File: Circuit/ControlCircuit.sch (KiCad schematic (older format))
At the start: 3 parts

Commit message: Schematics and PCB work
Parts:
- added C101: 4uF, Capacitors_SMD:C_0805, symbol CP1
- added C102: 32pF, Capacitors_SMD:C_0805, symbol C
- added C103: CP1, symbol CP1
- added D101: D_Schottky, symbol D_Schottky
- added L101: 260mH, symbol L
- added R101: 18kR, Resistors_SMD:R_0805, symbol R
- added R102: 11kR, Resistors_SMD:R_0805, symbol R
- added R103: 1.5R, Resistors_SMD:R_0805, symbol R
- added VR101: MC34063A, symbol MC34063A
- IC101: renamed from IC?; footprint DIL28 -> Housings_DIP:DIP-28_W7.62mm
- LCD101: renamed from LCD?; footprint (none) -> Pin_Headers:Pin_Header_Straight_2x20_Pitch2.54mm
- R104: renamed from R?; footprint (none) -> Resistors_SMD:R_0805
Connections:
- net GNDREF is gone; now on net GND: LCD101.1 (LEDK), LCD101.10 (DB15), LCD101.11 (DB14), LCD101.12 (DB13), LCD101.13 (DB12), LCD101.14 (DB11), LCD101.15 (DB10), LCD101.16 (DB9), LCD101.17 (DB8), LCD101.18 (DB7), LCD101.19 (DB6), LCD101.20 (DB5), LCD101.21 (DB4), LCD101.22 (DB3), LCD101.23 (DB2), LCD101.24 (DB1), LCD101.25 (DB0), LCD101.26 (GND), LCD101.8 (DB17), LCD101.9 (DB16)
- net +3V3: now also LCD101.39 (3.3V), LCD101.4 (IM3), LCD101.5 (IM2), LCD101.6 (IM1), C101.1, D101.1 (K), L101.1, VR101.2 (Switch_Emitter)
- net CS: now also LCD101.32 (CS)
- net MISO: now also LCD101.27 (SDO)
- net MOSI: now also LCD101.28 (SDI)
- net SCK: now also LCD101.31 (RS)
- net WR: now also LCD101.30 (WR)
- net GND: now reaches LCD101.29 (RD)
- net GND: now also LCD101.3 (IM0), LCD101.33 (TE), LCD101.34 (GND), LCD101.40 (GND), C101.2, C102.1, C103.2, D101.2 (A), R102.1, VR101.4 (Grid)
- net X+: now reaches LCD101.35 (X+)
- net Y+: now reaches LCD101.36 (Y+)
- net X-: now reaches LCD101.37 (X-)
- net Y-: now reaches LCD101.38 (Y-)
- net RST: now reaches LCD101.7 (RST)
- new net: R103.2, VR101.1 (Switch_Collector), VR101.7 (Ipk_Sense), VR101.8 (Driver_Collector)
- new net: C102.2, VR101.3 (Timing_Capacitor)
- new net: R101.1, R102.2, VR101.5 (Comp_Inv_Input)
- new net: L101.2, R101.2
- new net +24V: R103.1, VR101.6 (Vcc)
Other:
- note added: "LCD + Touch screen"
- note added: "Relay Inputs, contains \nglobal labels Input1..6"
- note added: "Relay Outputs, contains \nglobal labels Output1..6"
- note added: "Voltage regulation and power supply"
- moved on the sheet: IC101, LCD101, R104

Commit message: Continued PCB work, placement started. Report and presentation also started
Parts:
- C103: value CP1 -> 100uF; footprint (none) -> Capacitors_SMD:C_0805
- D101: footprint (none) -> Diodes_SMD:D_0805
- L101: footprint (none) -> Inductors:Inductor_1212
- VR101: footprint (none) -> Housings_DIP:DIP-8_W7.62mm
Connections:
- net +24V: now also C103.1
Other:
- moved on the sheet: C103
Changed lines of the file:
@@
 EESchema Schematic File Version 2
+LIBS:ControlCircuit-rescue
 LIBS:power
 LIBS:device
@@
 F 0 "VR101" H 9100 4750 60  0000 C CNN
 F 1 "MC34063A" H 9100 4150 60  0000 C CNN
-F 2 "" H 8200 4600 60  0001 C CNN
+F 2 "Housings_DIP:DIP-8_W7.62mm" H 8200 4600 60  0001 C CNN
 F 3 "" H 8200 4600 60  0001 C CNN
 	1    9100 4450
@@
 F 0 "L101" V 8500 5100 50  0000 C CNN
 F 1 "260mH" V 8625 5100 50  0000 C CNN
-F 2 "" H 8550 5100 50  0001 C CNN
+F 2 "Inductors:Inductor_1212" H 8550 5100 50  0001 C CNN
 F 3 "" H 8550 5100 50  0000 C CNN
 	1    8550 5100
@@
 L CP1 C103
 U 1 1 58ADC4C2
-P 10300 4650
-F 0 "C103" H 10325 4750 50  0000 L CNN
-F 1 "CP1" H 10325 4550 50  0000 L CNN
-F 2 "" H 10300 4650 50  0001 C CNN
-F 3 "" H 10300 4650 50  0000 C CNN
-	1    10300 4650
+P 10300 4750
+F 0 "C103" H 10325 4850 50  0000 L CNN
+F 1 "100uF" H 10325 4650 50  0000 L CNN
+F 2 "Capacitors_SMD:C_0805" H 10300 4750 50  0001 C CNN
+F 3 "" H 10300 4750 50  0000 C CNN
+	1    10300 4750
 	1    0    0    -1
 $EndComp
@@
 F 0 "D101" H 7400 4500 50  0000 C CNN
 F 1 "D_Schottky" H 7400 4300 50  0000 C CNN
-F 2 "" H 7400 4400 50  0001 C CNN
+F 2 "Diodes_SMD:D_0805" H 7400 4400 50  0001 C CNN
 F 3 "" H 7400 4400 50  0000 C CNN
 	1    7400 4400
@@
 L GND #PWR012
 U 1 1 58ADCA05
-P 10300 4800
-F 0 "#PWR012" H 10300 4550 50  0001 C CNN
-F 1 "GND" H 10300 4650 50  0000 C CNN
-F 2 "" H 10300 4800 50  0000 C CNN
-F 3 "" H 10300 4800 50  0000 C CNN
-	1    10300 4800
+P 10300 5000
+F 0 "#PWR012" H 10300 4750 50  0001 C CNN
+F 1 "GND" H 10300 4850 50  0000 C CNN
+F 2 "" H 10300 5000 50  0000 C CNN
+F 3 "" H 10300 5000 50  0000 C CNN
+	1    10300 5000
 	1    0    0    -1
 $EndComp
@@
 Wire Notes Line
 	3650 650  2450 650
+Wire Wire Line
+	10300 4600 10300 4500
+Connection ~ 10300 4500
+Wire Wire Line
+	10300 4900 10300 5000
 $EndSCHEMATC

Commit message: Continued PCB work, additional footprints added
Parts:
- removed IC101: ATMEGA328-P, Housings_DIP:DIP-28_W7.62mm, symbol ATMEGA328-P
- removed LCD101: tft-proto-mi0283qt-9a, Pin_Headers:Pin_Header_Straight_2x20_Pitch2.54mm, symbol tft-proto-mi0283qt-9a
- removed R104: 100R, Resistors_SMD:R_0805, symbol R
- D101: footprint Diodes_SMD:D_0805 -> Diodes_SMD:D_MiniMELF_Standard
- L101: footprint Inductors:Inductor_1212 -> Inductors:Inductor_Wurth_HCI-7050
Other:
- note removed: "LCD + Touch screen"
- note removed: "Relay Inputs, contains \nglobal labels Input1..6"
- note removed: "Relay Outputs, contains \nglobal labels Output1..6"

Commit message: Additional PCB work
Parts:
- added P101, P102, P103, P104: CONN_01X08, Connectors_Terminal_Blocks:TerminalBlock_Pheonix_MKDS1.5-8pol, symbol CONN_01X08
- added P105: CONN_01X02, Connectors_Terminal_Blocks:TerminalBlock_Pheonix_MKDS1.5-2pol, symbol CONN_01X02
- VR101: footprint Housings_DIP:DIP-8_W7.62mm -> Housings_SOIC:SOIC-8_3.9x4.9mm_Pitch1.27mm
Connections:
- net labels added: OR6s1, OR6s2, OR7c, OR7s2, OR8c, OR8s2
- wire segments 28 -> 127

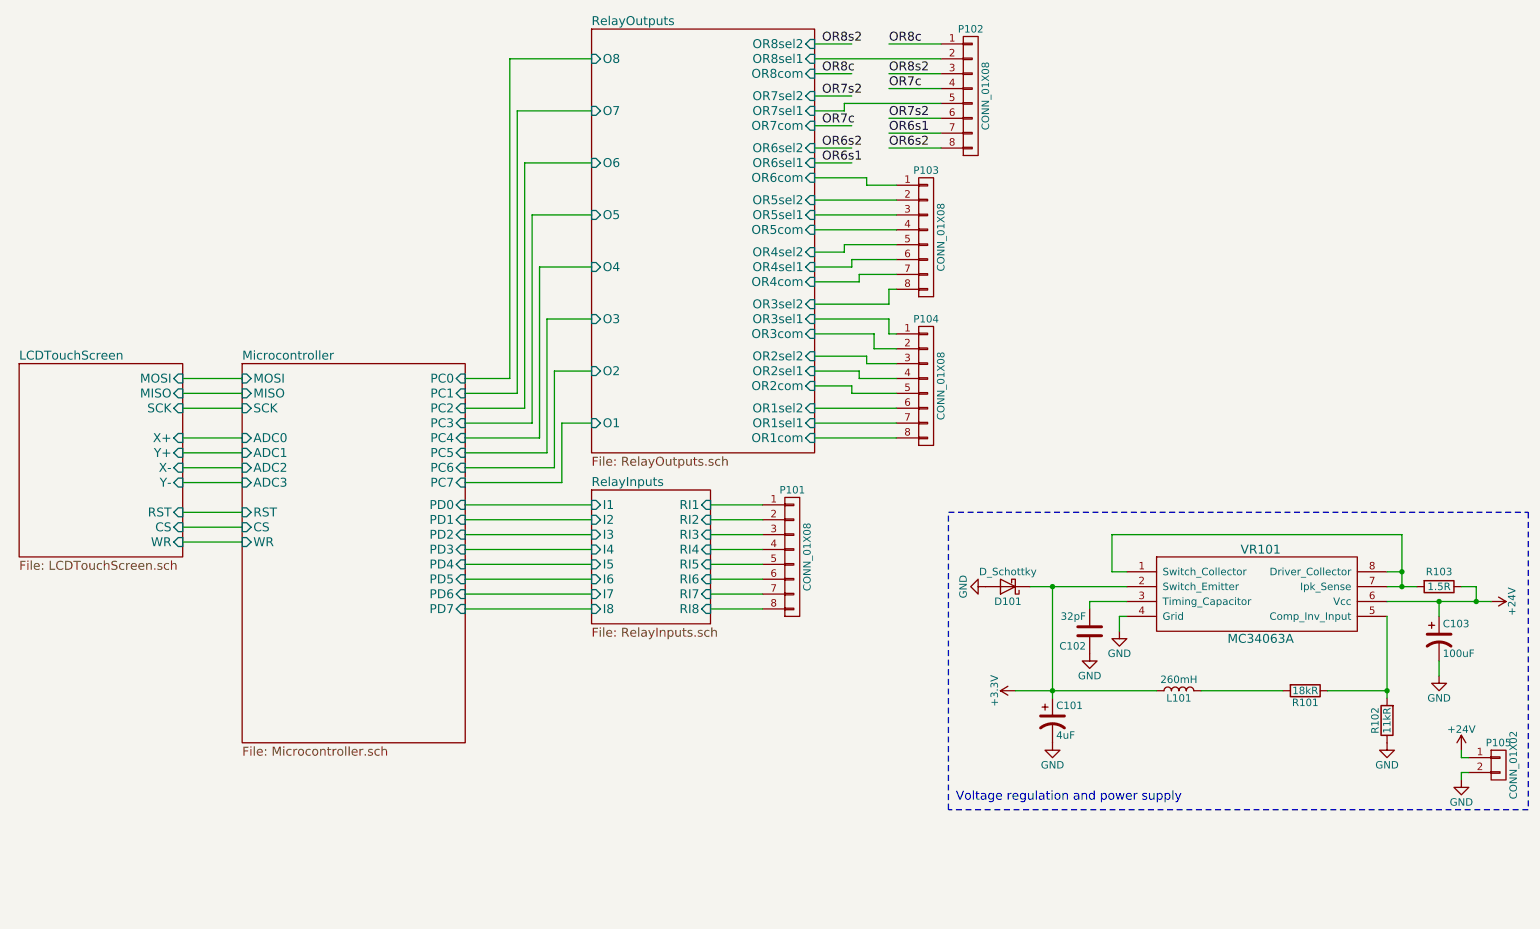
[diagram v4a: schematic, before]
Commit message: Routed PCB and made backup. Footprint for Optocouplers
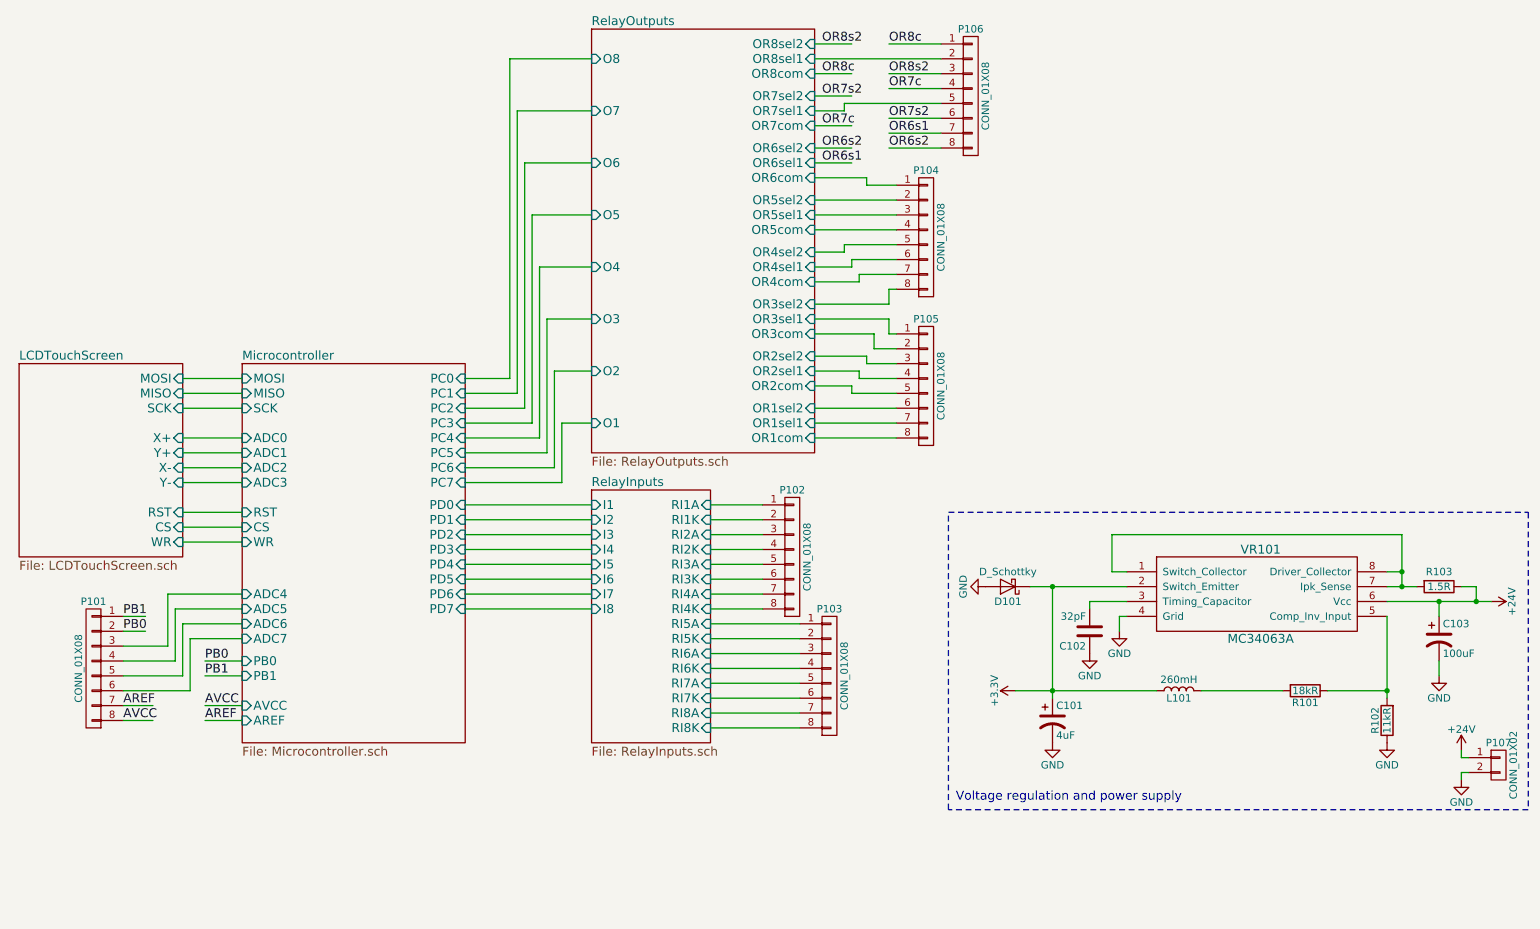
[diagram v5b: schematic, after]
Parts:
- added P101, P103: CONN_01X08, Connectors_Terminal_Blocks:TerminalBlock_Pheonix_MKDS1.5-8pol, symbol CONN_01X08
- renumbered P101 to P102, P103 to P104, P104 to P105, P102 to P106, P105 to P107
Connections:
- net labels added: AREF, AVCC, PB0, PB1
- wire segments 127 -> 155

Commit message: PCB. Pours mostly complete. Almost done?
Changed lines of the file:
@@
 F 3 "" H 10700 5600 50  0000 C CNN
 	1    10700 5600
-	1    0    0    -1
+	1    0    0    1
 $EndComp
 $Comp

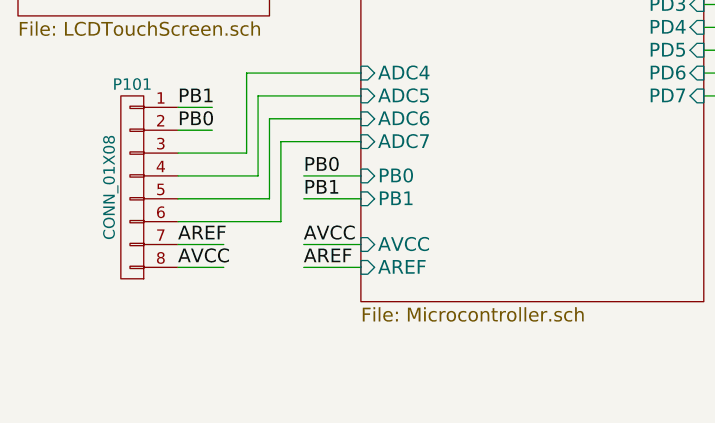
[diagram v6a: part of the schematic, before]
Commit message: Cleaned up silkscreen. Everything connected.
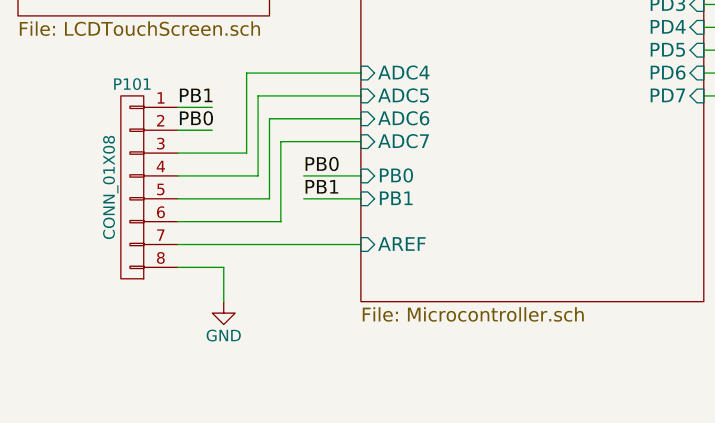
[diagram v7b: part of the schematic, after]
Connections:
- net labels removed: AREF, AVCC
- wire segments 155 -> 154
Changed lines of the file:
@@
 F32 "PB0" I L 2250 4900 60
 F33 "PB1" I L 2250 5000 60
-F34 "AVCC" I L 2250 5200 60
-F35 "AREF" I L 2250 5300 60
+F34 "AREF" I L 2250 5200 60
 $EndSheet
 $Comp
@@
 	1750 4800 1450 4800
 Wire Wire Line
-	1450 5200 1650 5200
+	1450 5200 2250 5200
 Wire Wire Line
 	1450 5300 1650 5300
 Wire Wire Line
-	2250 5200 2000 5200
-Wire Wire Line
-	2250 5300 2000 5300
-Text Label 2000 5200 0    60   ~ 0
-AVCC
-Text Label 2000 5300 0    60   ~ 0
-AREF
-Text Label 1450 5200 0    60   ~ 0
-AREF
-Text Label 1450 5300 0    60   ~ 0
-AVCC
+	1650 5300 1650 5450
+$Comp
+L GND #PWR?
+U 1 1 58B98A53
+P 1650 5450
+F 0 "#PWR?" H 1650 5200 50  0001 C CNN
+F 1 "GND" H 1650 5300 50  0000 C CNN
+F 2 "" H 1650 5450 50  0000 C CNN
+F 3 "" H 1650 5450 50  0000 C CNN
+	1    1650 5450
+	1    0    0    -1
+$EndComp
 $EndSCHEMATC

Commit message: PCB Revision 1
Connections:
- net labels added: PB3, PB4
- net labels removed: PB0, PB1
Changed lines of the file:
@@
 F30 "ADC6" I L 2250 4650 60
 F31 "ADC7" I L 2250 4750 60
-F32 "PB0" I L 2250 4900 60
-F33 "PB1" I L 2250 5000 60
-F34 "AREF" I L 2250 5200 60
+F32 "AREF" I L 2250 5200 60
+F33 "PB3" I L 2250 4900 60
+F34 "PB4" I L 2250 5000 60
 $EndSheet
 $Comp
@@
 Wire Wire Line
 	1450 4600 1600 4600
+Text Label 1450 4600 0    60   ~ 0
+PB4
 Text Label 1450 4700 0    60   ~ 0
-PB0
-Text Label 1450 4600 0    60   ~ 0
-PB1
+PB3
 Text Label 2000 4900 0    60   ~ 0
-PB0
+PB3
 Text Label 2000 5000 0    60   ~ 0
-PB1
+PB4
 Wire Wire Line
 	1750 4450 2250 4450
@@
 	1650 5300 1650 5450
 $Comp
-L GND #PWR?
+L GND #PWR011
 U 1 1 58B98A53
 P 1650 5450
-F 0 "#PWR?" H 1650 5200 50  0001 C CNN
+F 0 "#PWR011" H 1650 5200 50  0001 C CNN
 F 1 "GND" H 1650 5300 50  0000 C CNN
 F 2 "" H 1650 5450 50  0000 C CNN
